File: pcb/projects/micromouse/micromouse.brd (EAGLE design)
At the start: 80 x 100 mm, 52 parts, among them M1 332-06, M2 332-06, U1 DSPIC33FJ64MC804-H/PT, U2 UA78M33CKCS, U3 UA78M05CKCS

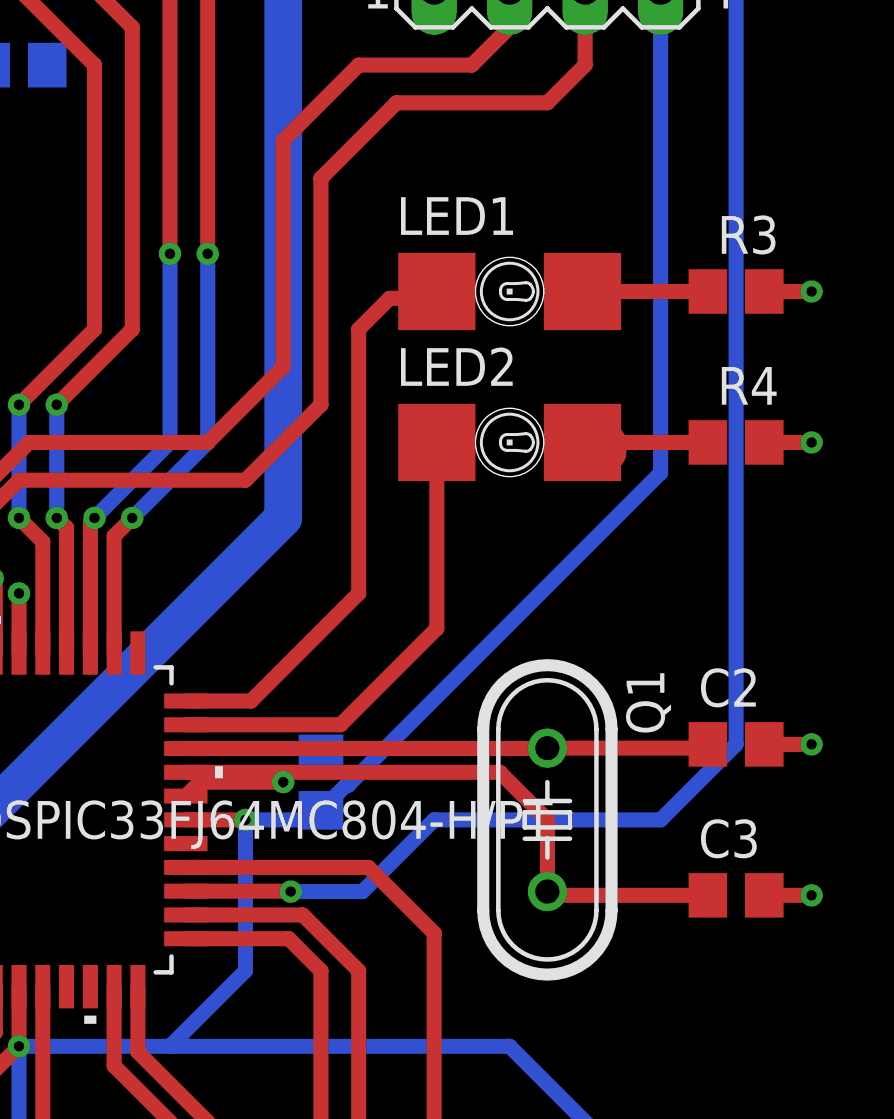
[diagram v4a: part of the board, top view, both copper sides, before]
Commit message: Replace LED with 0805 package
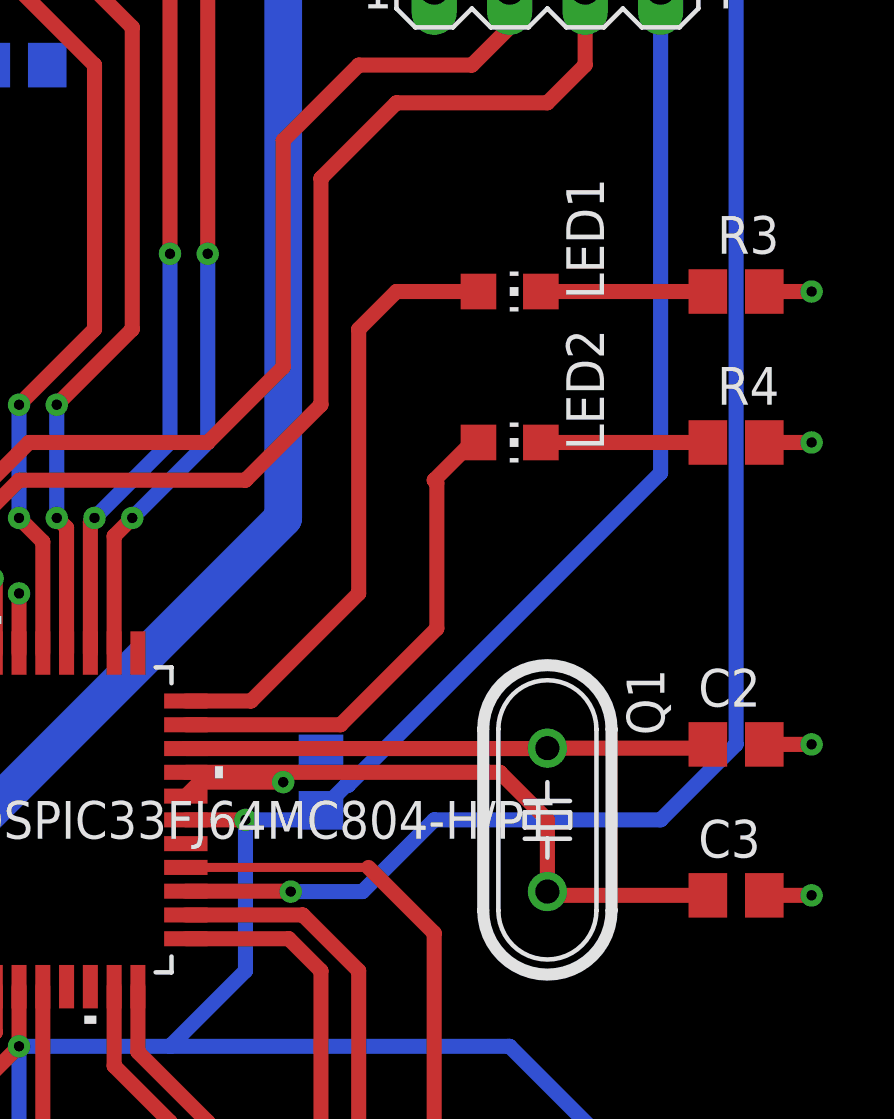
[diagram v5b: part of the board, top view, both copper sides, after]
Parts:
- LED1, LED2: value LAP4-TOP -> (none); device led:P47F-TOP -> led:CHIP-LED0805
- turned LED1 to 270 degrees
- turned LED2 to 270 degrees
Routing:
- net LED1: track 19.4 -> 20.8 mm
- net N$13: track 6.54 -> 5.62 mm
- net LED2: track 16.0 -> 16.8 mm
- net N$12: track 4.88 -> 5.62 mm
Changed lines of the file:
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@@
 </layers>
 <board>
-<fusionsync huburn="a.YnVzaW5lc3M6bXl0dW03NTE" projecturn="a.YnVzaW5lc3M6bXl0dW03NTEjMjAyMjAxMTg0ODY2MTA4MzE" f3durn="urn:adsk.wipprod:dm.lineage:0fkBe2gqQnChnMdfLTDDww" pcbguid="" lastpulledtime="2022-01-21T13:45:10Z" lastsyncedchangeguid="" latestrevisionid="d8952573-d15d-462f-b6d5-a90ccb888422" lastsyncedrevisionid="d8952573-d15d-462f-b6d5-a90ccb888422" lastboardhashguid="" lastpushedtime="" linktopcb3d="true"/>
+<fusionsync huburn="a.YnVzaW5lc3M6bXl0dW03NTE" projecturn="a.YnVzaW5lc3M6bXl0dW03NTEjMjAyMjAxMTg0ODY2MTA4MzE" f3durn="urn:adsk.wipprod:dm.lineage:0fkBe2gqQnChnMdfLTDDww" pcbguid="" lastpulledtime="2022-01-21T13:45:10Z" lastsyncedchangeguid="" latestrevisionid="6a0397da-a106-4a81-945a-c83413a9f04e" lastsyncedrevisionid="6a0397da-a106-4a81-945a-c83413a9f04e" lastboardhashguid="eefc5839-d65c-dcc0-8c7d-7e0dee3f5582" lastpushedtime="2022-01-25T12:08:33Z" linktopcb3d="true"/>
 <plain>
 <hole x="50" y="97" drill="2.2"/>
@@
 <attribute name="VALUE" x="17.4293" y="66.04" size="1.27" layer="27" rot="R270" align="top-center"/>
 </element>
-<element name="LED1" library="led" library_urn="urn:adsk.eagle:library:259" package="P47F-TOP" package3d_urn="urn:adsk.eagle:package:15879/1" value="LAP4-TOP" x="57.15" y="54.61" smashed="yes">
-<attribute name="NAME" x="53.34" y="56.515" size="1.27" layer="25"/>
-<attribute name="POPULARITY" value="0" x="128.27" y="16.51" size="1.778" layer="27" display="off"/>
-<attribute name="VALUE" x="53.34" y="51.435" size="1.27" layer="27"/>
-</element>
-<element name="LED2" library="led" library_urn="urn:adsk.eagle:library:259" package="P47F-TOP" package3d_urn="urn:adsk.eagle:package:15879/1" value="LAP4-TOP" x="57.15" y="49.53" smashed="yes">
-<attribute name="NAME" x="53.34" y="51.435" size="1.27" layer="25"/>
-<attribute name="POPULARITY" value="0" x="76.2" y="-3.81" size="1.778" layer="27" display="off"/>
-<attribute name="VALUE" x="53.34" y="46.355" size="1.27" layer="27"/>
+<element name="LED1" library="led" library_urn="urn:adsk.eagle:library:259" package="CHIP-LED0805" package3d_urn="urn:adsk.eagle:package:15818/2" value="" x="57.15" y="54.61" smashed="yes" rot="R270">
+<attribute name="NAME" x="59.055" y="58.42" size="1.27" layer="25" rot="R270"/>
+<attribute name="POPULARITY" value="68" x="19.05" y="-16.51" size="1.778" layer="27" rot="R270" display="off"/>
+<attribute name="VALUE" x="53.975" y="58.42" size="1.27" layer="27" rot="R270"/>
+</element>
+<element name="LED2" library="led" library_urn="urn:adsk.eagle:library:259" package="CHIP-LED0805" package3d_urn="urn:adsk.eagle:package:15818/2" value="" x="57.15" y="49.53" smashed="yes" rot="R270">
+<attribute name="NAME" x="59.055" y="53.34" size="1.27" layer="25" rot="R270"/>
+<attribute name="POPULARITY" value="68" x="3.81" y="30.48" size="1.778" layer="27" rot="R270" display="off"/>
+<attribute name="VALUE" x="53.975" y="53.34" size="1.27" layer="27" rot="R270"/>
 </element>
 <element name="M1" library="con-garry" library_urn="urn:adsk.eagle:library:147" package="332-06" package3d_urn="urn:adsk.eagle:package:6811/1" value="332-06" x="33.02" y="78.74" smashed="yes" rot="R90">
@@
 <contactref element="R2" pad="2"/>
 <contactref element="U1" pad="26"/>
-<wire x1="46.2534" y1="35.23" x2="52.4" y2="35.23" width="0.508" layer="1"/>
-<wire x1="52.4" y1="35.23" x2="54.61" y2="33.02" width="0.508" layer="1"/>
+<wire x1="54.61" y1="33.02" x2="52.4" y2="35.23" width="0.508" layer="1"/>
 <wire x1="54.61" y1="33.02" x2="54.61" y2="25.4" width="0.508" layer="1"/>
 <wire x1="54.61" y1="25.4" x2="54.61" y2="22.54" width="0.508" layer="1"/>
 <wire x1="58.9788" y1="23.8506" x2="56.1594" y2="23.8506" width="0.508" layer="1"/>
 <wire x1="56.1594" y1="23.8506" x2="54.61" y2="25.4" width="0.508" layer="1"/>
+<wire x1="52.4" y1="35.23" x2="46.2534" y2="35.23" width="0.3048" layer="1"/>
 </signal>
 <signal name="LED1">
@@
 <wire x1="46.2534" y1="40.83" x2="48.45" y2="40.83" width="0.508" layer="1"/>
 <wire x1="48.45" y1="40.83" x2="52.07" y2="44.45" width="0.508" layer="1"/>
-<wire x1="52.07" y1="44.45" x2="52.07" y2="53.34" width="0.508" layer="1"/>
-<wire x1="54.3211375" y1="54.3794" x2="54.5517375" y2="54.61" width="0.508" layer="1"/>
-<wire x1="54.5517375" y1="54.61" x2="54.7" y2="54.61" width="0.508" layer="1"/>
-<wire x1="52.07" y1="53.34" x2="53.1094" y2="54.3794" width="0.508" layer="1"/>
-<wire x1="53.1094" y1="54.3794" x2="54.3211375" y2="54.3794" width="0.508" layer="1"/>
+<wire x1="52.07" y1="53.34" x2="52.07" y2="44.45" width="0.508" layer="1"/>
+<wire x1="56.1" y1="54.61" x2="53.34" y2="54.61" width="0.508" layer="1"/>
+<wire x1="53.34" y1="54.61" x2="52.07" y2="53.34" width="0.508" layer="1"/>
 </signal>
 <signal name="LED2">
@@
 <contactref element="U1" pad="32"/>
 <wire x1="46.2534" y1="40.03" x2="51.46" y2="40.03" width="0.508" layer="1"/>
-<wire x1="54.7" y1="43.27" x2="54.7" y2="49.53" width="0.508" layer="1"/>
 <wire x1="51.46" y1="40.03" x2="54.7" y2="43.27" width="0.508" layer="1"/>
+<wire x1="54.7" y1="43.27" x2="54.7" y2="48.17" width="0.508" layer="1"/>
+<wire x1="54.7" y1="48.17" x2="54.61" y2="48.26" width="0.508" layer="1"/>
+<wire x1="54.61" y1="48.26" x2="55.88" y2="49.53" width="0.508" layer="1"/>
+<wire x1="55.88" y1="49.53" x2="56.1" y2="49.53" width="0.508" layer="1"/>
 </signal>
 <signal name="N$12">
 <contactref element="LED1" pad="C"/>
 <contactref element="R3" pad="1"/>
-<wire x1="59.8214375" y1="54.2083" x2="59.6" y2="54.2083" width="0.508" layer="1"/>
-<wire x1="63.82" y1="54.61" x2="60.2231375" y2="54.61" width="0.508" layer="1"/>
-<wire x1="60.2231375" y1="54.61" x2="59.8214375" y2="54.2083" width="0.508" layer="1"/>
-<wire x1="59.6" y1="54.61" x2="59.8214375" y2="54.3885625" width="0.508" layer="1"/>
-<wire x1="59.8214375" y1="54.3885625" x2="59.8214375" y2="54.2083" width="0.508" layer="1"/>
+<wire x1="58.2" y1="54.61" x2="63.82" y2="54.61" width="0.508" layer="1"/>
 </signal>
 <signal name="N$13">
 <contactref element="LED2" pad="C"/>
 <contactref element="R4" pad="1"/>
-<wire x1="60.4405" y1="49.53" x2="60.4405" y2="49.20855" width="1.27" layer="1"/>
-<wire x1="60.4405" y1="49.20855" x2="60.180975" y2="48.949025" width="1.27" layer="1"/>
-<wire x1="59.8214375" y1="49.1283" x2="59.6" y2="49.1283" width="0.508" layer="1"/>
-<wire x1="63.82" y1="49.53" x2="60.2231375" y2="49.53" width="0.508" layer="1"/>
-<wire x1="60.2231375" y1="49.53" x2="59.8214375" y2="49.1283" width="0.508" layer="1"/>
-<wire x1="59.6" y1="49.53" x2="59.8214375" y2="49.3085625" width="0.508" layer="1"/>
-<wire x1="59.8214375" y1="49.3085625" x2="59.8214375" y2="49.1283" width="0.508" layer="1"/>
-<wire x1="59.6" y1="49.53" x2="59.92145" y2="49.20855" width="0.508" layer="1"/>
-<wire x1="59.92145" y1="49.20855" x2="60.4405" y2="49.20855" width="0.508" layer="1"/>
+<wire x1="58.2" y1="49.53" x2="63.82" y2="49.53" width="0.508" layer="1"/>
 </signal>
 </signals>
